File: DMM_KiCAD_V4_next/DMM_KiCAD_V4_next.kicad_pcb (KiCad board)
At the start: 4 copper layers, 68.5 x 53.2 mm, 76 parts, among them J1 Conn_01x07_Pin, J10 ANALOG, J11 I_Input, J12 Conn_01x02_Pin, J13 DIGITAL1, J14 Barrel_Jack, J15 Barrel_Jack, J16 Conn_01x01_Socket, J17 Conn_01x01_Socket, J2 MicoSD, J3 Conn_01x07_Pin, J5 POWER2, J6 POWER1, J7 Conn_01x02_Pin, J8 DIGITAL2, J9 Out to Screen, Q1 MMBT3904, Q2 AO3400A MOSFET, Q6 BSS138, Q7 BSS138, Q8 AO3400A MOSFET, SW1 SW_Push, SW2 SW_Push, SW3 SW_SPDT, SW4 SW_Push, U1 LM317_TO-220, U10 LM4040DBZ-2.5, U11 LM4040DBZ-5, U12 TLV61046ADBVR, U2 IX4426N, U3 ADS1115IDGS, U4 IX4426N, U5 Opamp_Dual, U7 MAX1683, U8 Opamp_Dual, U9 TPS613222ADBV

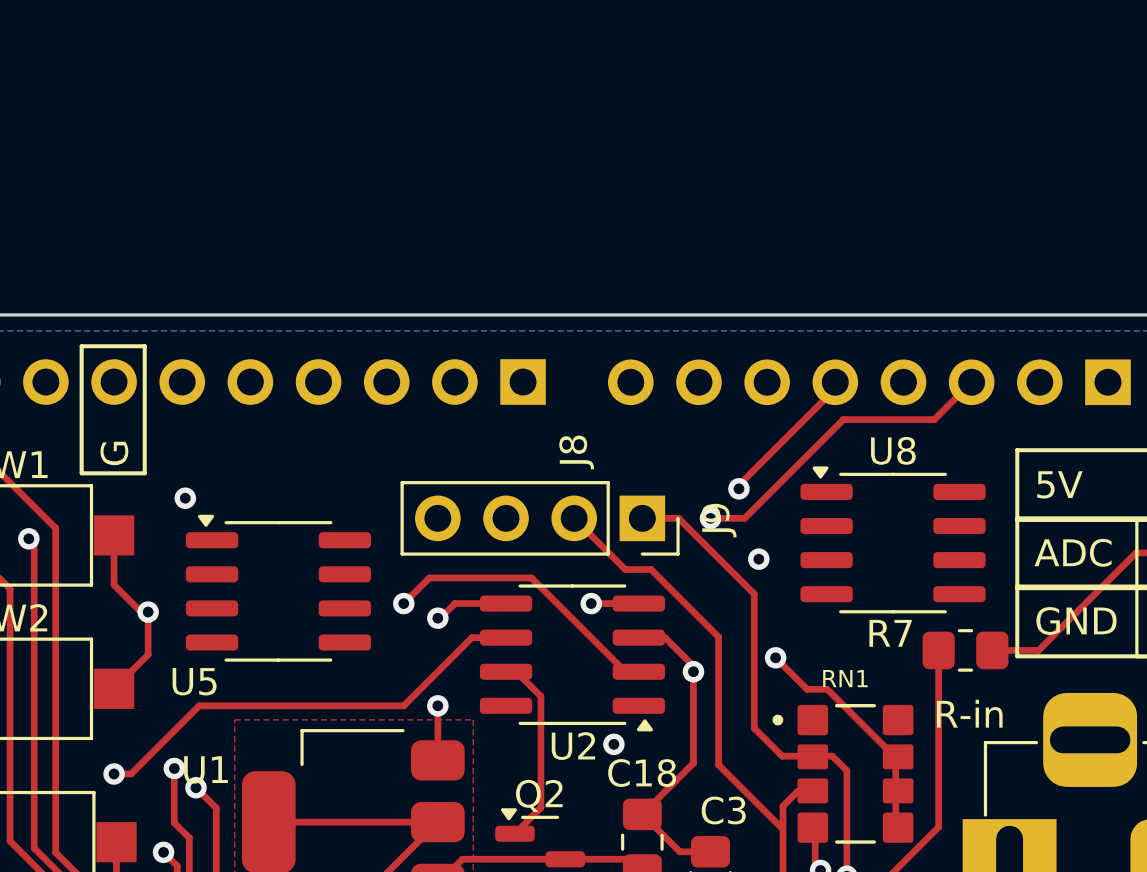
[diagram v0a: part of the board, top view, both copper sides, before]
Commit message: Giga Open Lead Detection Revisions & Minor PCB edits
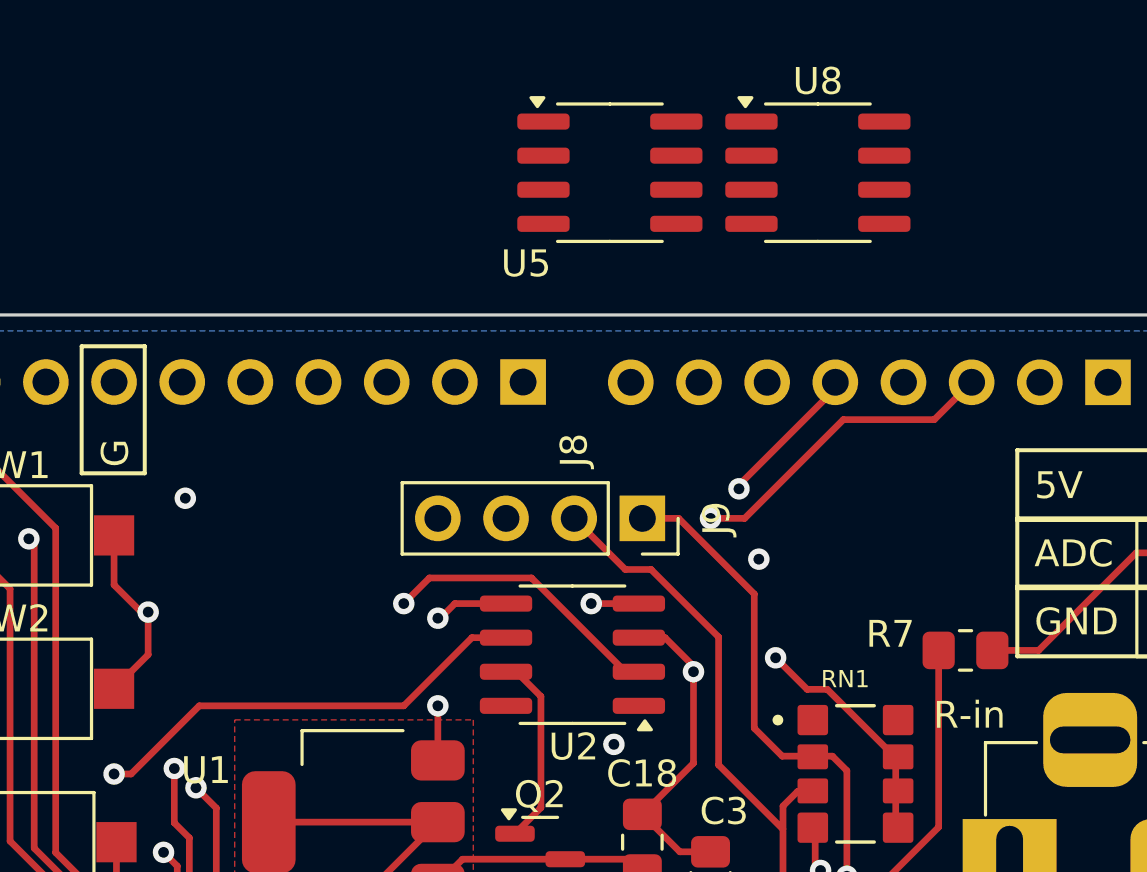
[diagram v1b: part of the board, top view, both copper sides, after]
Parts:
- moved U5 19.9 mm to (123.2, 43.0)
- moved U8 14.1 mm to (131.0, 43.0)
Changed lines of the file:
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@@
 	(footprint "Package_SO:SOIC-8_3.9x4.9mm_P1.27mm"
 		(layer "F.Cu")
-		(at 110.9 58.6)
+		(at 123.25 43)
 		(descr "SOIC, 8 Pin (JEDEC MS-012AA, https://www.analog.com/media/en/package-pcb-resources/package/pkg_pdf/soic_narrow-r/r_8.pdf), generated with kicad-footprint-generator ipc_gullwing_generator.py")
 		(tags "SOIC SO")
@@
 	(footprint "Package_SO:SOIC-8_3.9x4.9mm_P1.27mm"
 		(layer "F.Cu")
-		(at 133.8 56.8)
+		(at 131 43)
 		(descr "SOIC, 8 Pin (JEDEC MS-012AA, https://www.analog.com/media/en/package-pcb-resources/package/pkg_pdf/soic_narrow-r/r_8.pdf), generated with kicad-footprint-generator ipc_gullwing_generator.py")
 		(tags "SOIC SO")

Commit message: New AdaLogger Version and PCB revisions
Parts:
- removed J2: MicoSD, Connector_PinSocket_2.54mm:PinSocket_1x06_P2.54mm_Vertical
- removed JP6: Jumper_2_Bridged, Jumper:SolderJumper-2_P1.3mm_Bridged_Pad1.0x1.5mm
- removed Q6, Q7: BSS138, Package_TO_SOT_SMD:SOT-23
- removed RN2: 10k x4, Library:RESCAXS127P508X320X70-8N
- added C7: 0.1uF, Capacitor_SMD:C_0805_2012Metric_Pad1.18x1.45mm_HandSolder, F.Cu at (50.7, 35.5)
- added C8: 0.1uF, Capacitor_SMD:C_0805_2012Metric_Pad1.18x1.45mm_HandSolder, F.Cu at (50.7, 38.5)
- added R12: 0, Resistor_SMD:R_0805_2012Metric_Pad1.20x1.40mm_HandSolder, F.Cu at (125.5, 76.0)
- added R22: 0, Resistor_SMD:R_0805_2012Metric_Pad1.20x1.40mm_HandSolder, F.Cu at (74.0, 54.5)
- added RN3: 10k x4, Library:RESCAXS127P508X320X70-8N, F.Cu at (61.5, 35.7)
- added RN4: 10k x4, Library:RESCAXS127P508X320X70-8N, F.Cu at (35.5, 48.5)
- added RN5: 10k x4, Library:RESCAXS127P508X320X70-8N, F.Cu at (40.1, 24.4)
- added U13: ISO1540, Package_SO:SOIC-8_3.9x4.9mm_P1.27mm, F.Cu at (61.8, 43.5)
- added U14: RFM-0505S, Converter_DCDC:Converter_DCDC_TRACO_TEA1-xxxx_THT, F.Cu at (111.2, 87.7)
- U5, U8: value Opamp_Dual -> LTV-824; footprint Package_SO:SOIC-8_3.9x4.9mm_P1.27mm -> Package_SO:SOP-8_6.605x9.655mm_P2.54mm
- moved U8 96.6 mm to (35.5, 57.5)
- moved U5 83.5 mm to (40.2, 33.5)
- moved R8 72.7 mm to (45.1, 84.2)
- moved U12 72.7 mm to (49.4, 81.7)
- moved C1 72.7 mm to (54.5, 85.2)
- moved C2 72.7 mm to (54.2, 81.7)
- moved C5 72.7 mm to (54.5, 88.2)
- moved C6 72.7 mm to (54.5, 91.0)
- moved L2 72.7 mm to (49.5, 76.0)
- moved R25 72.7 mm to (49.5, 85.5)
- moved U4 18.7 mm to (118.2, 77.8)
- moved R22 15.9 mm to (103.0, 92.8)
- moved R23 0.17 mm to (113.5, 94.6)
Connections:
- C10 pad 1: GND -> Gnd-iso
- C17 pad 1: GND -> Gnd-iso
- C18 pad 2: GND -> Gnd-iso
- C3 pad 2: GND -> Gnd-iso
- C4 pad 1: GND -> Gnd-iso
- C4 pad 2: VDD -> 5V-iso
- D4 pad 1: VDD -> 5V-iso
- D5 pad 2: GND -> Gnd-iso
- F1 pad 2: GND -> Gnd-iso
- J11 pad 1: VDD -> 5V-iso
- J11 pad 3: GND -> Gnd-iso
- R27 pad 1: VDD -> 5V-iso
- R6 pad 1: GND -> Gnd-iso
- RN1 pad 5: VDD -> 5V-iso
- RN1 pad 6: VDD -> 5V-iso
- RN1 pad 7: VDD -> 5V-iso
- U10 pad 2: GND -> Gnd-iso
- U10 pad 3: GND -> Gnd-iso
- U11 pad 2: GND -> Gnd-iso
- U11 pad 3: GND -> Gnd-iso
- U2 pad 2: D7 -> /Driver_U2_In_A
- U2 pad 3: GND -> Gnd-iso
- U2 pad 4: D9~ -> /Driver_U2_In_B
- U3 pad 3: GND -> Gnd-iso
- U3 pad 8: VDD -> 5V-iso
- U4 pad 2: D5~ (IR) -> /Driver_U4_In_A
- U4 pad 3: GND -> Gnd-iso
- U5 pad 1: unconnected-(U5-Pad1) -> D7
- U5 pad 2: unconnected-(U5A---Pad2) -> Net-(RN5-R1.1)
- U5 pad 3: unconnected-(U5A-+-Pad3) -> D9~
- U5 pad 4: unconnected-(U5C-V--Pad4) -> Net-(RN5-R2.1)
- U5 pad 5: unconnected-(U5B-+-Pad5) -> /Driver_U2_In_B
- U5 pad 6: unconnected-(U5B---Pad6) -> 5V-iso
- U5 pad 7: unconnected-(U5-Pad7) -> /Driver_U2_In_A
- U5 pad 8: unconnected-(U5C-V+-Pad8) -> 5V-iso
- U7 pad 1: GND -> Gnd-iso
- U7 pad 4: VDD -> 5V-iso
- U8 pad 1: unconnected-(U8-Pad1) -> D5~ (IR)
- U8 pad 2: unconnected-(U8A---Pad2) -> Net-(RN4-R1.1)
- U8 pad 4: unconnected-(U8C-V--Pad4) -> Net-(RN4-R2.1)
- U8 pad 5: unconnected-(U8B-+-Pad5) -> /Driver_U4_In_B
- U8 pad 6: unconnected-(U8B---Pad6) -> 5V-iso
- U8 pad 7: unconnected-(U8-Pad7) -> /Driver_U4_In_A
- U8 pad 8: unconnected-(U8C-V+-Pad8) -> 5V-iso
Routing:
- net VDD: track 149.1 -> 7.84 mm, vias 9 -> 0
- net 5V-iso: track 0.00 -> 71.1 mm, vias 0 -> 4
- net +3V3: track 69.7 -> 0.00 mm, vias 3 -> 0
- net GND: track 64.1 -> 10.9 mm, vias 14 -> 4
- net CLK: track 39.9 -> 0.00 mm, vias 1 -> 0
- net CS: track 39.2 -> 0.00 mm, vias 1 -> 0
- net MISO: track 39.1 -> 0.00 mm, vias 1 -> 0
- net MOSI: track 39.1 -> 0.00 mm, vias 1 -> 0
- net Gnd-iso: track 0.00 -> 37.1 mm, vias 0 -> 6
- net SDA: track 79.7 -> 54.7 mm, vias 4 -> 1
- net SCL-5V: track 45.7 -> 21.8 mm, vias 3 -> 0
- net SDA-5V: track 38.8 -> 20.3 mm, vias 2 -> 0
- net SCL: track 68.3 -> 50.6 mm, vias 3 -> 1
- net ADS_ADDR: track 11.4 -> 4.99 mm
- net /Uno5vPin: track 7.32 -> 5.53 mm
- added copper zone on In1.Cu, net GND
- added copper zone on In1.Cu, net Gnd-iso
- removed copper zone on B.Cu, net GND
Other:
- outline, holes or cut-outs redrawn
- board text added: "OIH Designs SMD DMM V6"
- board text removed: "CLK"
- board text removed: "CS"
- board text removed: "MISO"
- board text removed: "MOSI"
- board text removed: "OIH Designs SMD DMM V5"
